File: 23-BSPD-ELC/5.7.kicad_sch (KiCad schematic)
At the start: 5 parts, among them Q1 Q_PMOS_GSD, Q2 Q_PMOS_GSD

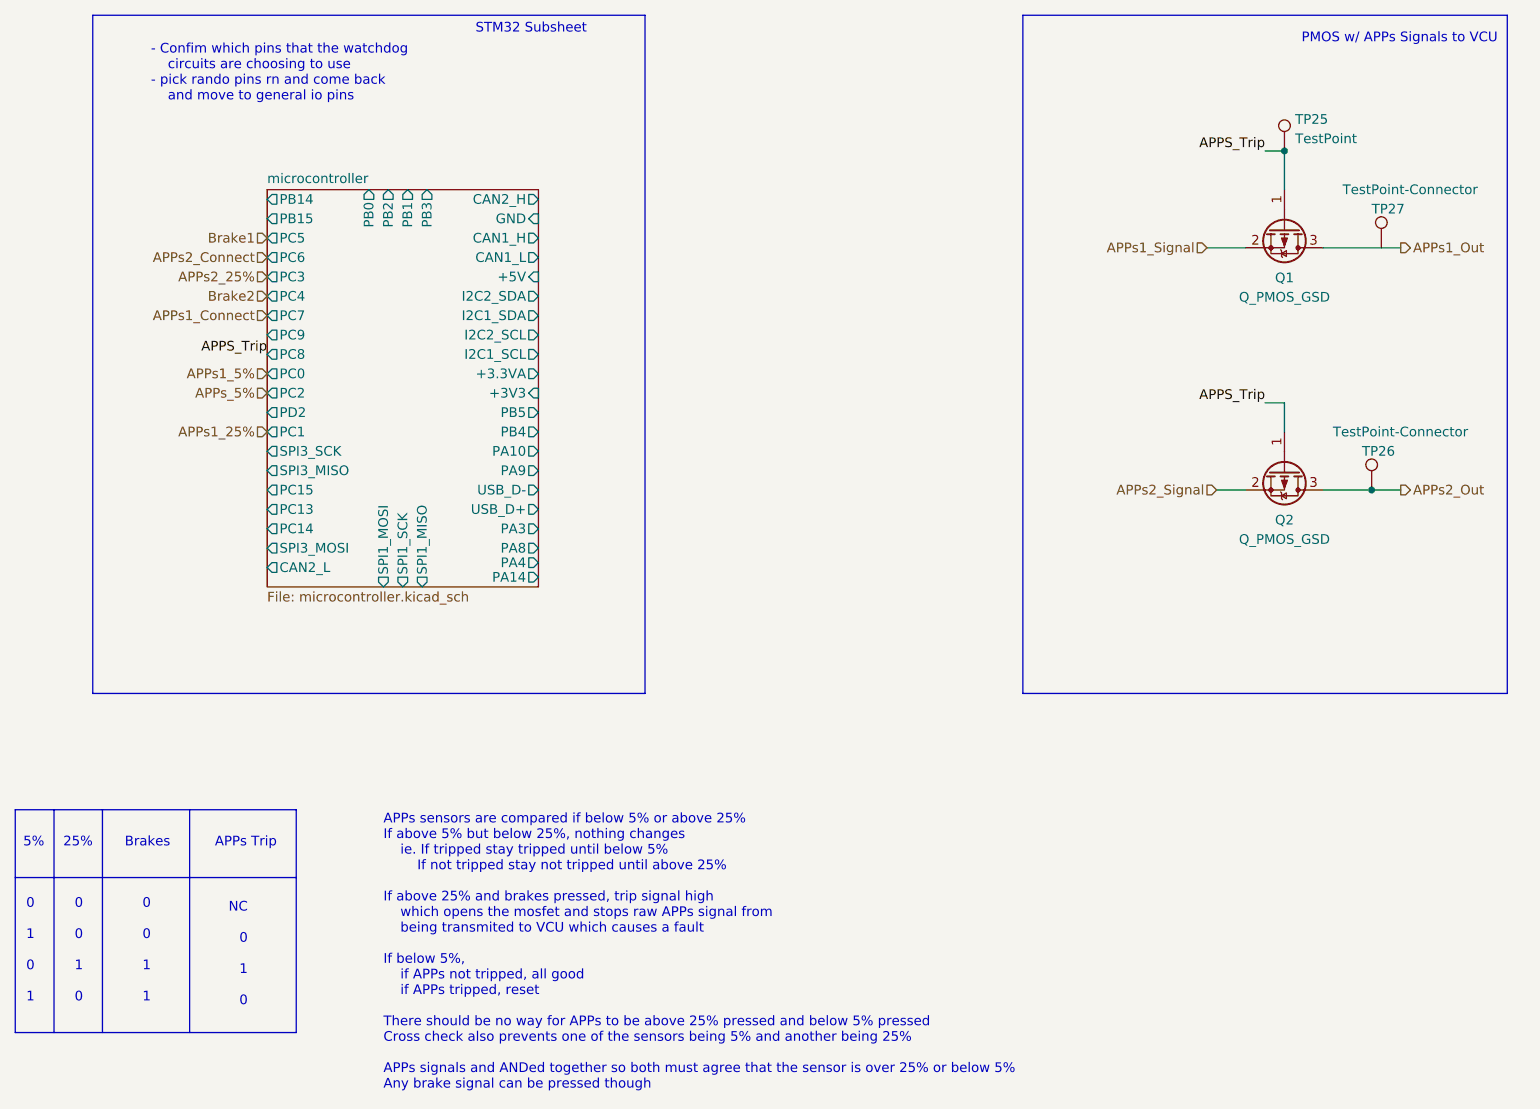
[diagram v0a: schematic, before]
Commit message: Revision changes and updates to some footprints
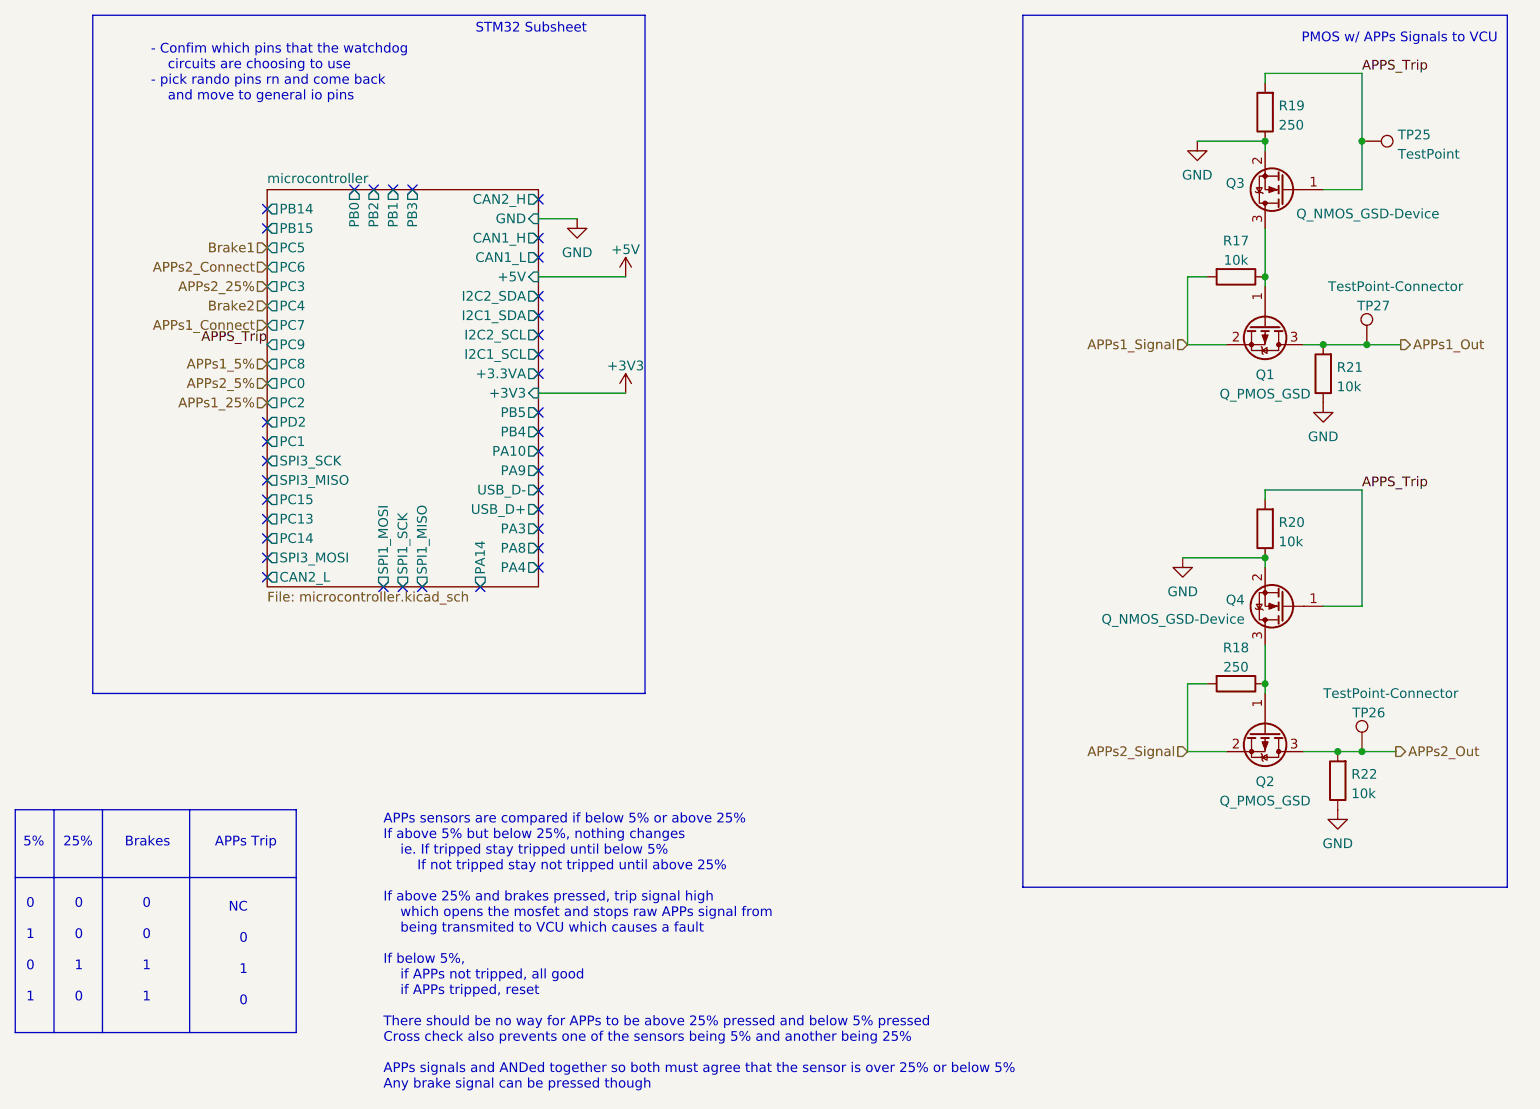
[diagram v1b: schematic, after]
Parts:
- added Q3, Q4: Q_NMOS_GSD-Device, symbol 20-ELC-2-01-R1(Appetizer)-rescue:Q_NMOS_GSD-Device
- added R17, R20, R21, R22: 10k, symbol Device:R
- added R18, R19: 250, symbol Device:R
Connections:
- net APPS_Trip: now also Q3.1 (G), Q4.1 (G), R19.2, R20.2; no longer Q1.1 (G), Q2.1 (G)
- net APPs1_Out: now also TP27.1, R21.2
- net APPs1_Signal: now also R17.2
- net APPs2_Out: now also R22.2
- net APPs2_Signal: now also R18.2
- new net: Q1.1 (G), Q3.3 (D), R17.1
- new net: Q2.1 (G), Q4.3 (D), R18.1
- new net GND: Q3.2 (S), Q4.2 (S), R19.1, R20.1, R21.1, R22.1
- no-connect marks 0 -> 36
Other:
- moved on the sheet: TP25, TP26, TP27

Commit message: Updated pcb layout; Watchdog on board still in progress
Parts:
- Q1, Q2, Q3, Q4: footprint (none) -> Package_TO_SOT_SMD:TSOT-23
- R17, R18, R19, R20, R21, R22: footprint (none) -> Resistor_SMD:R_0603_1608Metric_Pad0.98x0.95mm_HandSolder
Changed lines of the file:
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@@
     (property "Reference" "R17" (id 0) (at 194.31 54.9742 90))
     (property "Value" "10k" (id 1) (at 194.31 57.5111 90))
-    (property "Footprint" "" (id 2) (at 194.31 57.912 90)
+    (property "Footprint" "Resistor_SMD:R_0603_1608Metric_Pad0.98x0.95mm_HandSolder" (id 2) (at 194.31 57.912 90)
       (effects (font (size 1.27 1.27)) hide)
     )
@@
       (effects (font (size 1.27 1.27)) (justify right))
     )
-    (property "Footprint" "" (id 2) (at 207.518 72.39 90)
+    (property "Footprint" "Resistor_SMD:R_0603_1608Metric_Pad0.98x0.95mm_HandSolder" (id 2) (at 207.518 72.39 90)
       (effects (font (size 1.27 1.27)) hide)
     )
@@
       (effects (font (size 1.27 1.27)) (justify left))
     )
-    (property "Footprint" "" (id 2) (at 195.58 105.41 0)
+    (property "Footprint" "Package_TO_SOT_SMD:TSOT-23" (id 2) (at 195.58 105.41 0)
       (effects (font (size 1.27 1.27)) hide)
     )
@@
       (effects (font (size 1.27 1.27)) (justify right))
     )
-    (property "Footprint" "" (id 2) (at 199.898 92.71 90)
+    (property "Footprint" "Resistor_SMD:R_0603_1608Metric_Pad0.98x0.95mm_HandSolder" (id 2) (at 199.898 92.71 90)
       (effects (font (size 1.27 1.27)) hide)
     )
@@
       (effects (font (size 1.27 1.27)) (justify right))
     )
-    (property "Footprint" "" (id 2) (at 199.898 38.1 90)
+    (property "Footprint" "Resistor_SMD:R_0603_1608Metric_Pad0.98x0.95mm_HandSolder" (id 2) (at 199.898 38.1 90)
       (effects (font (size 1.27 1.27)) hide)
     )
@@
     (property "Reference" "Q2" (id 0) (at 198.12 125.8554 90))
     (property "Value" "Q_PMOS_GSD" (id 1) (at 198.12 128.3923 90))
-    (property "Footprint" "" (id 2) (at 200.66 124.46 0)
+    (property "Footprint" "Package_TO_SOT_SMD:TSOT-23" (id 2) (at 200.66 124.46 0)
       (effects (font (size 1.27 1.27)) hide)
     )
@@
     (property "Reference" "R18" (id 0) (at 194.31 108.3142 90))
     (property "Value" "250" (id 1) (at 194.31 110.8511 90))
-    (property "Footprint" "" (id 2) (at 194.31 111.252 90)
+    (property "Footprint" "Resistor_SMD:R_0603_1608Metric_Pad0.98x0.95mm_HandSolder" (id 2) (at 194.31 111.252 90)
       (effects (font (size 1.27 1.27)) hide)
     )
@@
       (effects (font (size 1.27 1.27)) (justify right))
     )
-    (property "Footprint" "" (id 2) (at 209.423 125.73 90)
+    (property "Footprint" "Resistor_SMD:R_0603_1608Metric_Pad0.98x0.95mm_HandSolder" (id 2) (at 209.423 125.73 90)
       (effects (font (size 1.27 1.27)) hide)
     )
@@
     (property "Reference" "Q1" (id 0) (at 198.12 72.5154 90))
     (property "Value" "Q_PMOS_GSD" (id 1) (at 198.12 75.0523 90))
-    (property "Footprint" "" (id 2) (at 200.66 71.12 0)
+    (property "Footprint" "Package_TO_SOT_SMD:TSOT-23" (id 2) (at 200.66 71.12 0)
       (effects (font (size 1.27 1.27)) hide)
     )
@@
       (effects (font (size 1.27 1.27)) (justify left))
     )
-    (property "Footprint" "" (id 2) (at 195.58 50.8 0)
-      (effects (font (size 1.27 1.27)) hide)
-    )
+    (property "Footprint" "Package_TO_SOT_SMD:TSOT-23" (id 2) (at 195.58 50.8 0)
+      (effects (font (size 1.27 1.27)) hide)
+    )

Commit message: BSPD layout
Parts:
- R19: value 250 -> 10k
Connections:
- no-connect marks 36 -> 32
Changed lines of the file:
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@@
   (no_connect (at 83.82 48.26))
   (no_connect (at 102.87 72.39))
-  (no_connect (at 102.87 69.85))
   (no_connect (at 95.25 100.33))
-  (no_connect (at 102.87 57.15))
-  (no_connect (at 102.87 54.61))
-  (no_connect (at 102.87 64.77))
   (no_connect (at 102.87 67.31))
   (no_connect (at 102.87 62.23))
@@
     (stroke (width 0) (type default) (color 0 0 0 0))
   )
-  (wire (pts (xy 102.87 52.07) (xy 107.95 52.07))
+  (wire (pts (xy 102.87 52.07) (xy 110.744 52.07))
     (stroke (width 0) (type default) (color 0 0 0 0))
   )
@@
     (effects (font (size 1.27 1.27)) (justify right))
   )
+  (hierarchical_label "Watchdog_SDA" (shape input) (at 102.87 64.77 0)
+    (effects (font (size 1.27 1.27)) (justify left))
+  )
   (hierarchical_label "Brake1" (shape input) (at 67.31 55.88 180)
     (effects (font (size 1.27 1.27)) (justify right))
@@
     (effects (font (size 1.27 1.27)) (justify right))
   )
+  (hierarchical_label "CANL" (shape input) (at 102.87 57.15 0)
+    (effects (font (size 1.27 1.27)) (justify left))
+  )
+  (hierarchical_label "CANH" (shape input) (at 102.87 54.61 0)
+    (effects (font (size 1.27 1.27)) (justify left))
+  )
   (hierarchical_label "APPs2_Connect" (shape input) (at 67.31 58.42 180)
     (effects (font (size 1.27 1.27)) (justify right))
+  )
+  (hierarchical_label "Watchdog_SCL" (shape input) (at 102.87 69.85 0)
+    (effects (font (size 1.27 1.27)) (justify left))
   )
   (symbol (lib_id "Device:R") (at 194.31 59.69 270) (unit 1)
@@
     (pin "2")
   )
-  (symbol (lib_id "power:GND") (at 107.95 52.07 0) (unit 1)
-    (in_bom yes) (on_board yes) (fields_autoplaced)
-    (property "Reference" "#PWR078" (id 0) (at 107.95 58.42 0)
-      (effects (font (size 1.27 1.27)) hide)
-    )
-    (property "Value" "GND" (id 1) (at 107.95 56.5134 0))
-    (property "Footprint" "" (id 2) (at 107.95 52.07 0)
-      (effects (font (size 1.27 1.27)) hide)
-    )
-    (property "Datasheet" "" (id 3) (at 107.95 52.07 0)
+  (symbol (lib_id "power:GND") (at 110.744 52.07 0) (unit 1)
+    (in_bom yes) (on_board yes) (fields_autoplaced)
+    (property "Reference" "#PWR078" (id 0) (at 110.744 58.42 0)
+      (effects (font (size 1.27 1.27)) hide)
+    )
+    (property "Value" "GND" (id 1) (at 110.744 56.5134 0))
+    (property "Footprint" "" (id 2) (at 110.744 52.07 0)
+      (effects (font (size 1.27 1.27)) hide)
+    )
+    (property "Datasheet" "" (id 3) (at 110.744 52.07 0)
       (effects (font (size 1.27 1.27)) hide)
     )
@@
       (effects (font (size 1.27 1.27)) (justify right))
     )
-    (property "Value" "250" (id 1) (at 199.898 39.8022 0)
-      (effects (font (size 1.27 1.27)) (justify right))
-    )
+    (property "Value" "10k" (id 1) (at 199.898 39.8022 0)
+      (effects (font (size 1.27 1.27)) (justify right))
+    )
